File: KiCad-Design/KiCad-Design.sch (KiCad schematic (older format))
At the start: 69 parts, among them J1 USB_B_Micro, J2 Battery, J3 SENSOR, J4 Ext, J5 SENSORS, J6 OLED, Q1 SI2301, Q2 SI2301, Q3 UMH3N, Q4 SI2307CDS-T1-GE3, SW1 MCU BLE Adv, SW2 MCU FLASH, SW3 MCU RESET, U1 PMBT3904, U2 BME280, U3 CP2104, U4 LTC4054ES5-4.2, U5 HDC1080, U6 BME680, U7 AP2112K-3.3, U8 ttgo-32-micro-symbols

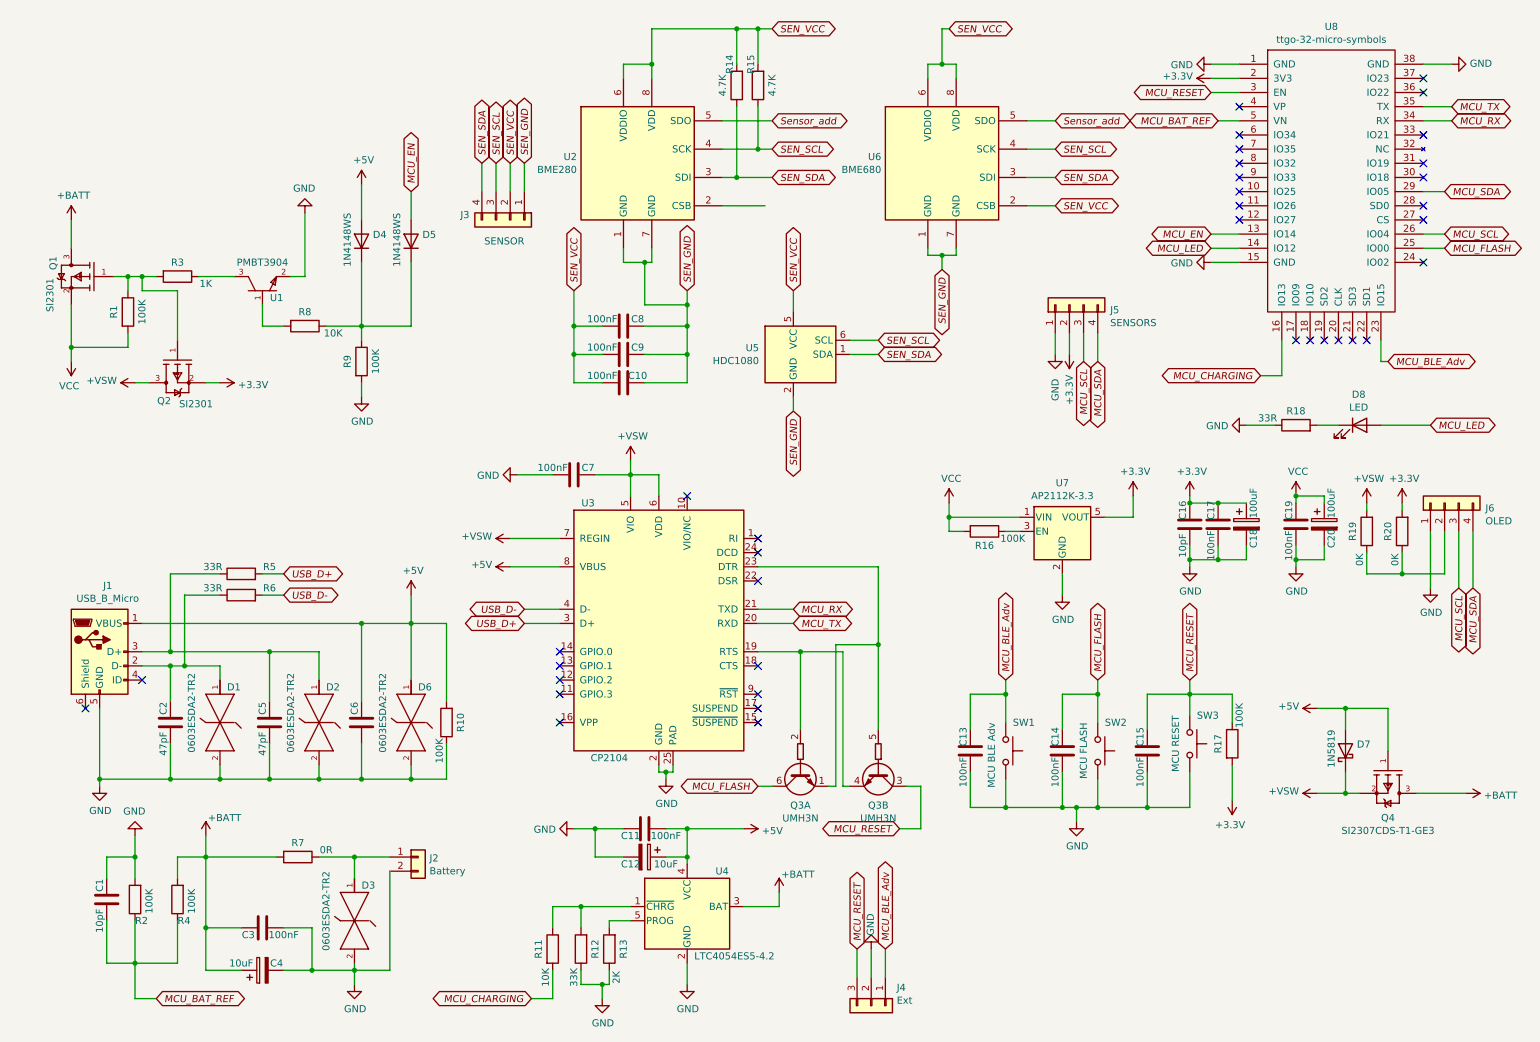
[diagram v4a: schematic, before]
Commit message: PCB: Moving the libraries to the project specific
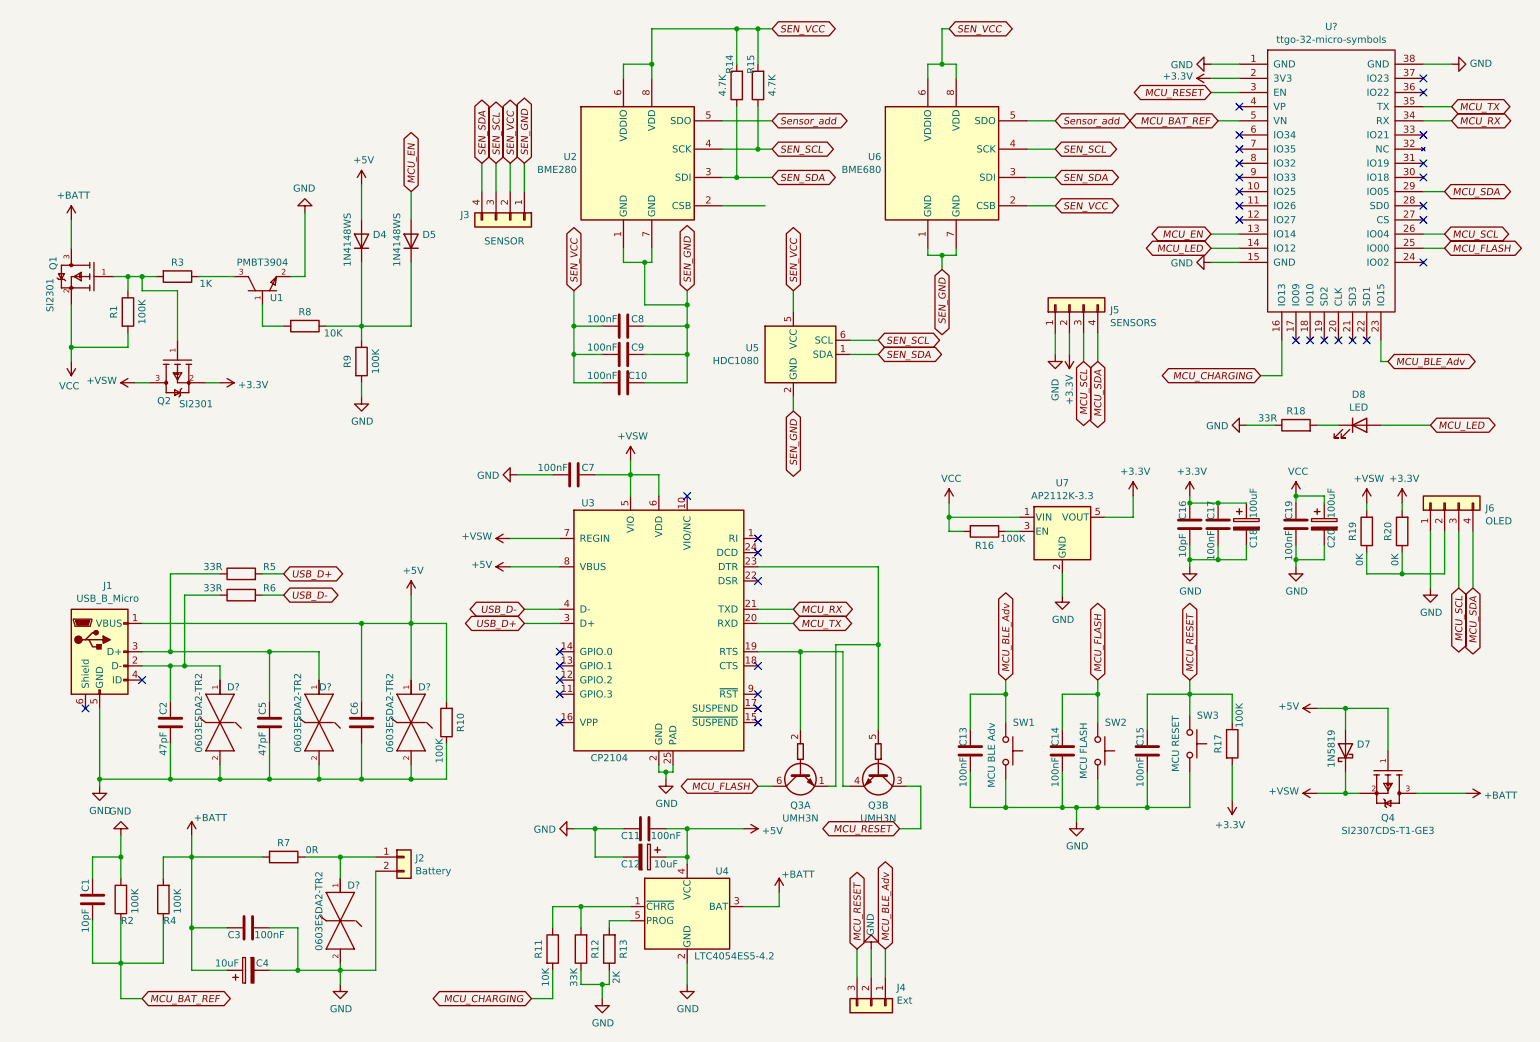
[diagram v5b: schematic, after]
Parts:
- removed D1, D2, D3, D6: 0603ESDA2-TR2, 0603ESDA2-TR2:Eaton-0603ESDA-0-0-0, symbol 0603ESDA2-TR2:0603ESDA2-TR2
- removed U8: ttgo-32-micro-symbols, ttgo-32-micro:TTGO-32-MICRO, symbol TTGO-32-MICRO:ttgo-32-micro-symbols
- added D? (x4): 0603ESDA2-TR2, 0603ESDA2-TR2:Eaton-0603ESDA-0-0-0, symbol 0603ESDA2:0603ESDA2-TR2
- added U?: ttgo-32-micro-symbols, symbol ttgo-32-micro:ttgo-32-micro-symbols
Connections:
- net +3V3: now also U?.2 (3V3)
- net +5V: now also D?.1
- net GND: now also D?.2, D?.2, D?.2, D?.2, U?.1 (GND), U?.15 (GND), U?.38 (GND)
- net MCU_BAT_REF: now also U?.5 (VN)
- net MCU_BLE_Adv: now also U?.23 (IO15)
- net MCU_CHARGING: now also U?.16 (IO13)
- net MCU_EN: now also U?.13 (IO14)
- net MCU_FLASH: now also U?.25 (IO00)
- net MCU_LED: now also U?.14 (IO12)
- net MCU_RESET: now also U?.3 (EN)
- net MCU_RX: now also U?.34 (RX)
- net MCU_SCL: now also U?.26 (IO04)
- net MCU_SDA: now also U?.29 (IO05)
- net MCU_TX: now also U?.35 (TX)
- net at J2.1 (Pin_1), R7.1: now also D?.1
- net at C2.2, J1.2 (D-), R6.1: now also D?.1
- net at C5.2, J1.3 (D+), R5.1: now also D?.1
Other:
- moved on the sheet: C1, C3, C4, J2, R2, R4, R7

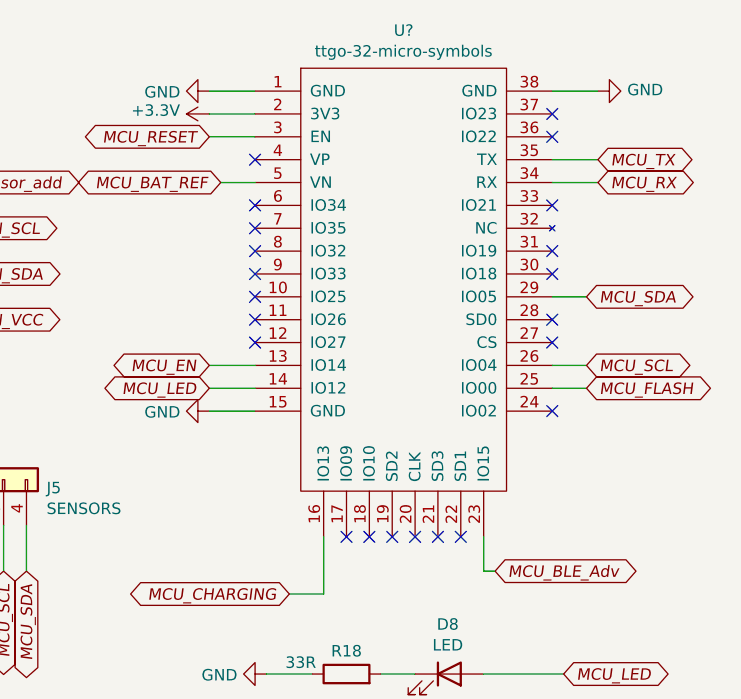
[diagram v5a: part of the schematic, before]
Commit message: PCB: Updating TTGO library
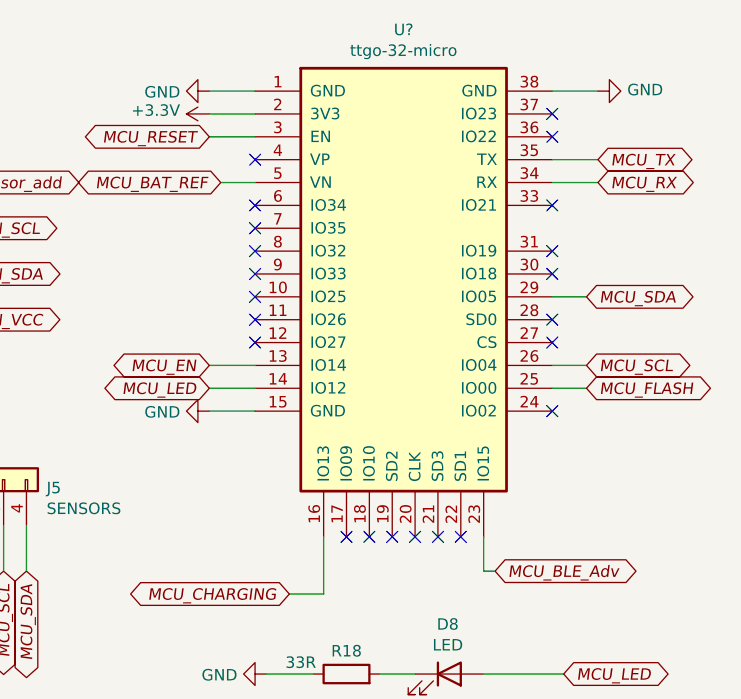
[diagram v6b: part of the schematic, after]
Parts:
- removed U?: ttgo-32-micro-symbols, symbol ttgo-32-micro:ttgo-32-micro-symbols
- added U?: ttgo-32-micro, open-Smartwatch:ttgo-32-micro, symbol ttgo-32-micro:ttgo-32-micro
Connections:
- net +3V3: now also U?.2 (3V3)
- net GND: now also U?.1 (GND), U?.15 (GND), U?.38 (GND)
- net MCU_BAT_REF: now also U?.5 (VN)
- net MCU_BLE_Adv: now also U?.23 (IO15)
- net MCU_CHARGING: now also U?.16 (IO13)
- net MCU_EN: now also U?.13 (IO14)
- net MCU_FLASH: now also U?.25 (IO00)
- net MCU_LED: now also U?.14 (IO12)
- net MCU_RESET: now also U?.3 (EN)
- net MCU_RX: now also U?.34 (RX)
- net MCU_SCL: now also U?.26 (IO04)
- net MCU_SDA: now also U?.29 (IO05)
- net MCU_TX: now also U?.35 (TX)
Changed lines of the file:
@@
 $EndComp
 $Comp
-L ttgo-32-micro:ttgo-32-micro-symbols U?
-U 1 1 606A549E
-P 9850 1600
-F 0 "U?" H 9850 2565 50  0000 C CNN
-F 1 "ttgo-32-micro-symbols" H 9850 2474 50  0000 C CNN
-F 2 "" H 9450 2200 50  0001 C CNN
-F 3 "" H 9450 2200 50  0001 C CNN
-	1    9850 1600
+L ttgo-32-micro:ttgo-32-micro U?
+U 1 1 60725496
+P 10100 1800
+F 0 "U?" H 9850 2968 50  0000 C CNN
+F 1 "ttgo-32-micro" H 9850 2877 50  0000 C CNN
+F 2 "open-Smartwatch:ttgo-32-micro" H 9800 2950 50  0001 C CNN
+F 3 "" H 9450 2600 50  0001 C CNN
+	1    10100 1800
 	1    0    0    -1
 $EndComp

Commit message: PCB: Re-validating the Schematic design
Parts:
- removed D4, D5: 1N4148WS, Diode_SMD:D_SOD-323, symbol Diode:1N4148WS
- removed D7: 1N5819, Diode_SMD:D_SOD-123, symbol Diode:1N5819
- removed Q1, Q2: SI2301, SI2301:Vishay-S-03946-07_2001-K-0, symbol SI2301:SI2301CDS-T1-GE3
- removed Q4: SI2307CDS-T1-GE3, SI2307:Vishay-S-03946-07_2001-K-IPC_B, symbol SI2307:SI2307CDS-T1-GE3
- removed R1, R9: 100K, Resistor_SMD:R_0805_2012Metric, symbol Device:R
- removed R3: 1K, Resistor_SMD:R_0805_2012Metric, symbol Device:R
- removed R8: 10K, Resistor_SMD:R_0805_2012Metric, symbol Device:R
- removed U1: PMBT3904, PMBT3904:NXP-PMBT3904,215-0, symbol PMBT3904:PMBT3904,215
- added D? (x2): 1N4148WS, Diode_SMD:D_SOD-323, symbol Diode:1N4148WS
- added R?: 1K, Resistor_SMD:R_0805_2012Metric, symbol Device:R
- added R?: 10K, Resistor_SMD:R_0805_2012Metric, symbol Device:R
- added R?: 33K, Resistor_SMD:R_0805_2012Metric, symbol Device:R
- added U?: AP2112K-3.3, Package_TO_SOT_SMD:SOT-23-5, symbol Regulator_Linear:AP2112K-3.3
- added U?: TPS2115A, TPS2115A:SON-8, symbol TPS2115A:TPS2115A
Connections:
- net +5V: now also U3.7 (REGIN), U?.6 (IN2)
- net +BATT: now also U?.2 (D0), U?.8 (IN1)
- net +VSW: now also D?.2 (A); no longer R19.2, U3.7 (REGIN)
- net GND: now also R?.2, R?.2, U?.3 (D1), U?.5 (GND)
- net MCU_EN: now also D?.2 (A)
- net VCC: now also R?.2, U?.1 (VIN), U?.2 (GND), U?.7 (OUT)
- net MCU_POWER_MODE: now reaches U?.6 (IO34)
- net MCU_POWER_MODE: now also R?.1, U?.1 (STAT)
- new net: D?.1 (K), D?.1 (K), R?.1, U?.3 (EN)
- new net: R?.1, U?.4 (ILIM)
- new net +3.3VA: R19.2, U?.5 (VOUT)
- no-connect marks 37 -> 36

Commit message: PCB: Updating the PCB design
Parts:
- D3, D4, D5, D6: renamed from D?; footprint 0603ESDA2-TR2:Eaton-0603ESDA-0-0-0 -> Eaton_0603ESDA2-TR2:Eaton-0603ESDA-0-0-0
- U9: renamed from U?; footprint open-Smartwatch:ttgo-32-micro -> ttgo-32-micro:TTGO-32-MICRO
- gave numbers to parts that had none: 7
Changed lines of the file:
@@
 	5050 650  5050 900
 $Comp
-L 0603ESDA2:0603ESDA2-TR2 D?
+L 0603ESDA2:0603ESDA2-TR2 D6
 U 1 1 6069A429
 P 3350 5150
-F 0 "D?" V 3500 5200 50  0000 L CNN
+F 0 "D6" V 3500 5200 50  0000 L CNN
 F 1 "0603ESDA2-TR2" H 3400 5000 50  0000 L CNN
-F 2 "0603ESDA2-TR2:Eaton-0603ESDA-0-0-0" H 3350 5650 50  0001 L CNN
+F 2 "Eaton_0603ESDA2-TR2:Eaton-0603ESDA-0-0-0" H 3350 5650 50  0001 L CNN
 F 3 "http://www.cooperindustries.com/content/dam/public/bussmann/Electronics/Resources/product-datasheets/bus-elx-ds-4419-0603esda2-tr2.pdf" H 3350 5750 50  0001 L CNN
 F 4 "Diode" H 3350 5850 50  0001 L CNN "category"
@@
 $EndComp
 $Comp
-L 0603ESDA2:0603ESDA2-TR2 D?
+L 0603ESDA2:0603ESDA2-TR2 D4
 U 1 1 6069F24E
 P 2700 5150
-F 0 "D?" V 2850 5150 50  0000 L CNN
+F 0 "D4" V 2850 5150 50  0000 L CNN
 F 1 "0603ESDA2-TR2" H 2750 5000 50  0000 L CNN
-F 2 "0603ESDA2-TR2:Eaton-0603ESDA-0-0-0" H 2700 5650 50  0001 L CNN
+F 2 "Eaton_0603ESDA2-TR2:Eaton-0603ESDA-0-0-0" H 2700 5650 50  0001 L CNN
 F 3 "http://www.cooperindustries.com/content/dam/public/bussmann/Electronics/Resources/product-datasheets/bus-elx-ds-4419-0603esda2-tr2.pdf" H 2700 5750 50  0001 L CNN
 F 4 "Diode" H 2700 5850 50  0001 L CNN "category"
@@
 $EndComp
 $Comp
-L 0603ESDA2:0603ESDA2-TR2 D?
+L 0603ESDA2:0603ESDA2-TR2 D3
 U 1 1 606A12D2
 P 2000 5150
-F 0 "D?" V 2150 5200 50  0000 L CNN
+F 0 "D3" V 2150 5200 50  0000 L CNN
 F 1 "0603ESDA2-TR2" H 2050 5000 50  0000 L CNN
-F 2 "0603ESDA2-TR2:Eaton-0603ESDA-0-0-0" H 2000 5650 50  0001 L CNN
+F 2 "Eaton_0603ESDA2-TR2:Eaton-0603ESDA-0-0-0" H 2000 5650 50  0001 L CNN
 F 3 "http://www.cooperindustries.com/content/dam/public/bussmann/Electronics/Resources/product-datasheets/bus-elx-ds-4419-0603esda2-tr2.pdf" H 2000 5750 50  0001 L CNN
 F 4 "Diode" H 2000 5850 50  0001 L CNN "category"
@@
 $EndComp
 $Comp
-L 0603ESDA2:0603ESDA2-TR2 D?
+L 0603ESDA2:0603ESDA2-TR2 D5
 U 1 1 606A2A83
 P 2850 6550
-F 0 "D?" V 3000 6600 50  0000 L CNN
+F 0 "D5" V 3000 6600 50  0000 L CNN
 F 1 "0603ESDA2-TR2" H 2900 6400 50  0000 L CNN
-F 2 "0603ESDA2-TR2:Eaton-0603ESDA-0-0-0" H 2850 7050 50  0001 L CNN
+F 2 "Eaton_0603ESDA2-TR2:Eaton-0603ESDA-0-0-0" H 2850 7050 50  0001 L CNN
 F 3 "http://www.cooperindustries.com/content/dam/public/bussmann/Electronics/Resources/product-datasheets/bus-elx-ds-4419-0603esda2-tr2.pdf" H 2850 7150 50  0001 L CNN
 F 4 "Diode" H 2850 7250 50  0001 L CNN "category"
@@
 $EndComp
 $Comp
-L ttgo-32-micro:ttgo-32-micro U?
+L ttgo-32-micro:ttgo-32-micro U9
 U 1 1 60725496
 P 10100 1800
-F 0 "U?" H 9850 2968 50  0000 C CNN
+F 0 "U9" H 9850 2968 50  0000 C CNN
 F 1 "ttgo-32-micro" H 9850 2877 50  0000 C CNN
-F 2 "open-Smartwatch:ttgo-32-micro" H 9800 2950 50  0001 C CNN
+F 2 "ttgo-32-micro:TTGO-32-MICRO" H 9800 2950 50  0001 C CNN
 F 3 "" H 9450 2600 50  0001 C CNN
 	1    10100 1800
@@
 $EndComp
 $Comp
-L Regulator_Linear:AP2112K-3.3 U?
+L Regulator_Linear:AP2112K-3.3 U8
 U 1 1 607663FB
 P 2350 1750
-F 0 "U?" H 2200 1500 50  0000 C CNN
+F 0 "U8" H 2200 1500 50  0000 C CNN
 F 1 "AP2112K-3.3" H 2350 2001 50  0000 C CNN
 F 2 "Package_TO_SOT_SMD:SOT-23-5" H 2350 2075 50  0001 C CNN
@@
 $EndComp
 $Comp
-L TPS2115A:TPS2115A U?
+L TPS2115A:TPS2115A U1
 U 1 1 607C18D5
 P 1450 3150
-F 0 "U?" H 1200 3600 50  0000 C CNN
+F 0 "U1" H 1200 3600 50  0000 C CNN
 F 1 "TPS2115A" H 1600 3600 50  0000 C CNN
 F 2 "TPS2115A:SON-8" H 1450 3700 50  0001 C CNN
@@
 	4250 4450 4400 4450
 $Comp
-L power:+5V #PWR?
+L power:+5V #PWR02
 U 1 1 607D9DBB
 P 900 2950
-F 0 "#PWR?" H 900 2800 50  0001 C CNN
+F 0 "#PWR02" H 900 2800 50  0001 C CNN
 F 1 "+5V" V 915 3077 50  0000 L CNN
 F 2 "" H 900 2950 50  0001 C CNN
@@
 $EndComp
 $Comp
-L power:GND #PWR?
+L power:GND #PWR08
 U 1 1 607DAA86
 P 900 3450
-F 0 "#PWR?" H 900 3200 50  0001 C CNN
+F 0 "#PWR08" H 900 3200 50  0001 C CNN
 F 1 "GND" V 905 3323 50  0000 R CNN
 F 2 "" H 900 3450 50  0001 C CNN
@@
 $EndComp
 $Comp
-L power:GND #PWR?
+L power:GND #PWR07
 U 1 1 607DAEEF
 P 900 3250
-F 0 "#PWR?" H 900 3000 50  0001 C CNN
+F 0 "#PWR07" H 900 3000 50  0001 C CNN
 F 1 "GND" V 905 3123 50  0000 R CNN
 F 2 "" H 900 3250 50  0001 C CNN
@@
 $EndComp
 $Comp
-L power:+BATT #PWR?
+L power:+BATT #PWR04
 U 1 1 607DEE0B
 P 900 3150
-F 0 "#PWR?" H 900 3000 50  0001 C CNN
+F 0 "#PWR04" H 900 3000 50  0001 C CNN
 F 1 "+BATT" V 900 3250 50  0000 L CNN
 F 2 "" H 900 3150 50  0001 C CNN
@@
 $EndComp
 $Comp
-L power:+BATT #PWR?
+L power:+BATT #PWR01
 U 1 1 607E1212
 P 900 2850
-F 0 "#PWR?" H 900 2700 50  0001 C CNN
+F 0 "#PWR01" H 900 2700 50  0001 C CNN
 F 1 "+BATT" V 900 2950 50  0000 L CNN
 F 2 "" H 900 2850 50  0001 C CNN
@@
 $EndComp
 $Comp
-L power:VCC #PWR?
+L power:VCC #PWR039
 U 1 1 607E212E
 P 2000 2850
-F 0 "#PWR?" H 2000 2700 50  0001 C CNN
+F 0 "#PWR039" H 2000 2700 50  0001 C CNN
 F 1 "VCC" H 2015 3023 50  0000 C CNN
 F 2 "" H 2000 2850 50  0001 C CNN
@@
 $EndComp
 $Comp
-L Device:R R?
+L Device:R R3
 U 1 1 607E44EA
 P 2050 3450
-F 0 "R?" V 2100 3300 50  0000 C CNN
+F 0 "R3" V 2100 3300 50  0000 C CNN
 F 1 "1K" V 2100 3600 50  0000 C CNN
 F 2 "Resistor_SMD:R_0805_2012Metric" V 1980 3450 50  0001 C CNN
@@
 $EndComp
 $Comp
-L power:GND #PWR?
+L power:GND #PWR040
 U 1 1 607FA807
 P 2050 3700
-F 0 "#PWR?" H 2050 3450 50  0001 C CNN
+F 0 "#PWR040" H 2050 3450 50  0001 C CNN
 F 1 "GND" V 2055 3573 50  0000 R CNN
 F 2 "" H 2050 3700 50  0001 C CNN
@@
 	1850 2850 2000 2850
 $Comp
-L Device:R R?
+L Device:R R8
 U 1 1 60897049
 P 2200 3450
-F 0 "R?" V 2250 3300 50  0000 C CNN
+F 0 "R8" V 2250 3300 50  0000 C CNN
 F 1 "10K" V 2250 3650 50  0000 C CNN
 F 2 "Resistor_SMD:R_0805_2012Metric" V 2130 3450 50  0001 C CNN
@@
 $EndComp
 $Comp
-L power:VCC #PWR?
+L power:VCC #PWR041
 U 1 1 60899174
 P 2200 3700
-F 0 "#PWR?" H 2200 3550 50  0001 C CNN
+F 0 "#PWR041" H 2200 3550 50  0001 C CNN
 F 1 "VCC" H 2215 3873 50  0000 C CNN
 F 2 "" H 2200 3700 50  0001 C CNN
@@
 	9200 1400 9100 1400
 $Comp
-L power:VCC #PWR?
+L power:VCC #PWR045
 U 1 1 60937D73
 P 2350 2150
-F 0 "#PWR?" H 2350 2000 50  0001 C CNN
+F 0 "#PWR045" H 2350 2000 50  0001 C CNN
 F 1 "VCC" H 2365 2323 50  0000 C CNN
 F 2 "" H 2350 2150 50  0001 C CNN
@@
 $EndComp
 $Comp
-L power:+VSW #PWR?
+L power:+VSW #PWR011
 U 1 1 60956F6D
 P 1050 1750
-F 0 "#PWR?" H 1050 1600 50  0001 C CNN
+F 0 "#PWR011" H 1050 1600 50  0001 C CNN
 F 1 "+VSW" V 1050 2000 50  0000 C CNN
 F 2 "" H 1050 1750 50  0001 C CNN
@@
 $EndComp
 $Comp
-L Diode:1N4148WS D?
+L Diode:1N4148WS D1
 U 1 1 6096E414
 P 1500 1750
-F 0 "D?" H 1350 1700 50  0000 C CNN
+F 0 "D1" H 1350 1700 50  0000 C CNN
 F 1 "1N4148WS" H 1750 1700 50  0000 C CNN
 F 2 "Diode_SMD:D_SOD-323" H 1500 1575 50  0001 C CNN
@@
 	1050 1750 1350 1750
 $Comp
-L power:VCC #PWR?
+L power:VCC #PWR010
 U 1 1 6099DFCE
 P 1050 1650
-F 0 "#PWR?" H 1050 1500 50  0001 C CNN
+F 0 "#PWR010" H 1050 1500 50  0001 C CNN
 F 1 "VCC" V 1050 1850 50  0000 C CNN
 F 2 "" H 1050 1650 50  0001 C CNN
@@
 $EndComp
 $Comp
-L Diode:1N4148WS D?
+L Diode:1N4148WS D2
 U 1 1 609B55F5
 P 1500 1900
-F 0 "D?" H 1350 1850 50  0000 C CNN
+F 0 "D2" H 1350 1850 50  0000 C CNN
 F 1 "1N4148WS" H 1750 1850 50  0000 C CNN
 F 2 "Diode_SMD:D_SOD-323" H 1500 1725 50  0001 C CNN
@@
 	1850 1750 2050 1750
 $Comp
-L power:GND #PWR?
+L power:GND #PWR013
 U 1 1 60A15744
 P 1050 2000
-F 0 "#PWR?" H 1050 1750 50  0001 C CNN
+F 0 "#PWR013" H 1050 1750 50  0001 C CNN
 F 1 "GND" V 1055 1873 50  0000 R CNN
 F 2 "" H 1050 2000 50  0001 C CNN
@@
 $EndComp
 $Comp
-L Device:R R?
+L Device:R R1
 U 1 1 60A16343
 P 1500 2000
-F 0 "R?" V 1550 1850 50  0000 C CNN
+F 0 "R1" V 1550 1850 50  0000 C CNN
 F 1 "33K" V 1550 2200 50  0000 C CNN
 F 2 "Resistor_SMD:R_0805_2012Metric" V 1430 2000 50  0001 C CNN
@@
 	2350 2050 2350 2150
 $Comp
-L power:+3.3VA #PWR?
+L power:+3.3VA #PWR046
 U 1 1 60A99936
 P 2850 1650
-F 0 "#PWR?" H 2850 1500 50  0001 C CNN
+F 0 "#PWR046" H 2850 1500 50  0001 C CNN
 F 1 "+3.3VA" V 2865 1778 50  0000 L CNN
 F 2 "" H 2850 1650 50  0001 C CNN
@@
 	2850 1650 2650 1650
 $Comp
-L power:+3.3VA #PWR?
+L power:+3.3VA #PWR047
 U 1 1 60AB66D2
 P 10100 4000
-F 0 "#PWR?" H 10100 3850 50  0001 C CNN
+F 0 "#PWR047" H 10100 3850 50  0001 C CNN
 F 1 "+3.3VA" H 10115 4173 50  0000 C CNN
 F 2 "" H 10100 4000 50  0001 C CNN
